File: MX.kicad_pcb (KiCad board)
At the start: 2 copper layers, 50.8 x 25.4 mm, 2 parts

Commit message: Fixed names
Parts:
- removed the SW** at (152.7, 88.9)
- added SW**: MX700H, Keyboard_switches:MX700H, F.Cu at (152.4, 88.9)
- moved LED** 0.25 mm to (152.4, 94.0)
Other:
- board size 50.8 x 25.4 mm -> 136.9 x 25.4 mm

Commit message: Upated MX700H and MX700HR
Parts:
- removed the SW** at (152.4, 88.9)
- added SW**: MX700HR, Keyboard_switches:MX700HR, F.Cu at (152.4, 88.9)

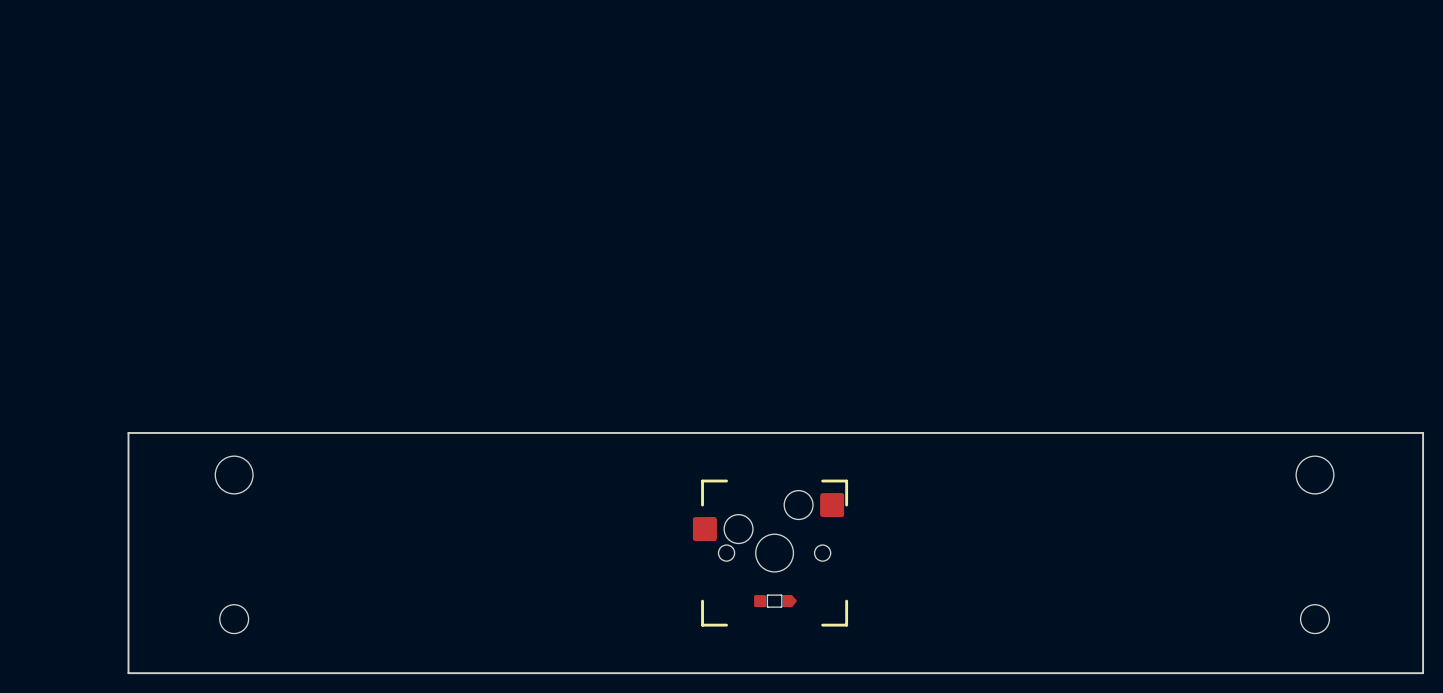
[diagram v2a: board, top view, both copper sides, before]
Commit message: Added symbols library
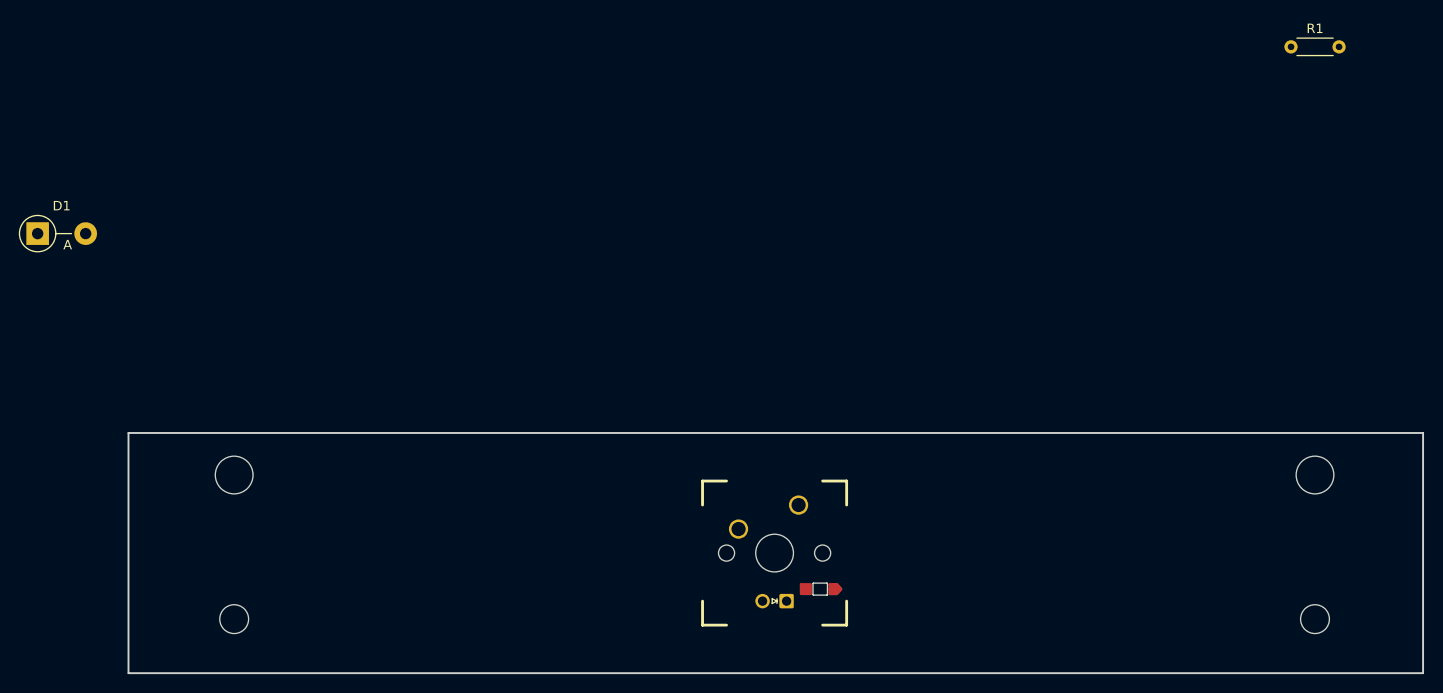
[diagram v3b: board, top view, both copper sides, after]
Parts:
- removed LED**: smdLed0805, Keyboard_switches:smdLed0805
- removed SW**: MX700HR, Keyboard_switches:MX700HR
- added D1: 1N4148, Diode_THT:D_DO-15_P5.08mm_Vertical_AnodeUp, F.Cu at (74.5, 55.1)
- added LED1: 0805, Keyboard_switches:smdLed0805, F.Cu at (157.2, 92.7)
- added R1: 100r, Resistor_THT:R_Axial_DIN0204_L3.6mm_D1.6mm_P5.08mm_Horizontal, F.Cu at (207.0, 35.4)
- added SW1: MXSwitch, Keyboard_switches:MX700R, F.Cu at (152.4, 88.9)

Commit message: Added support for THT LEDs
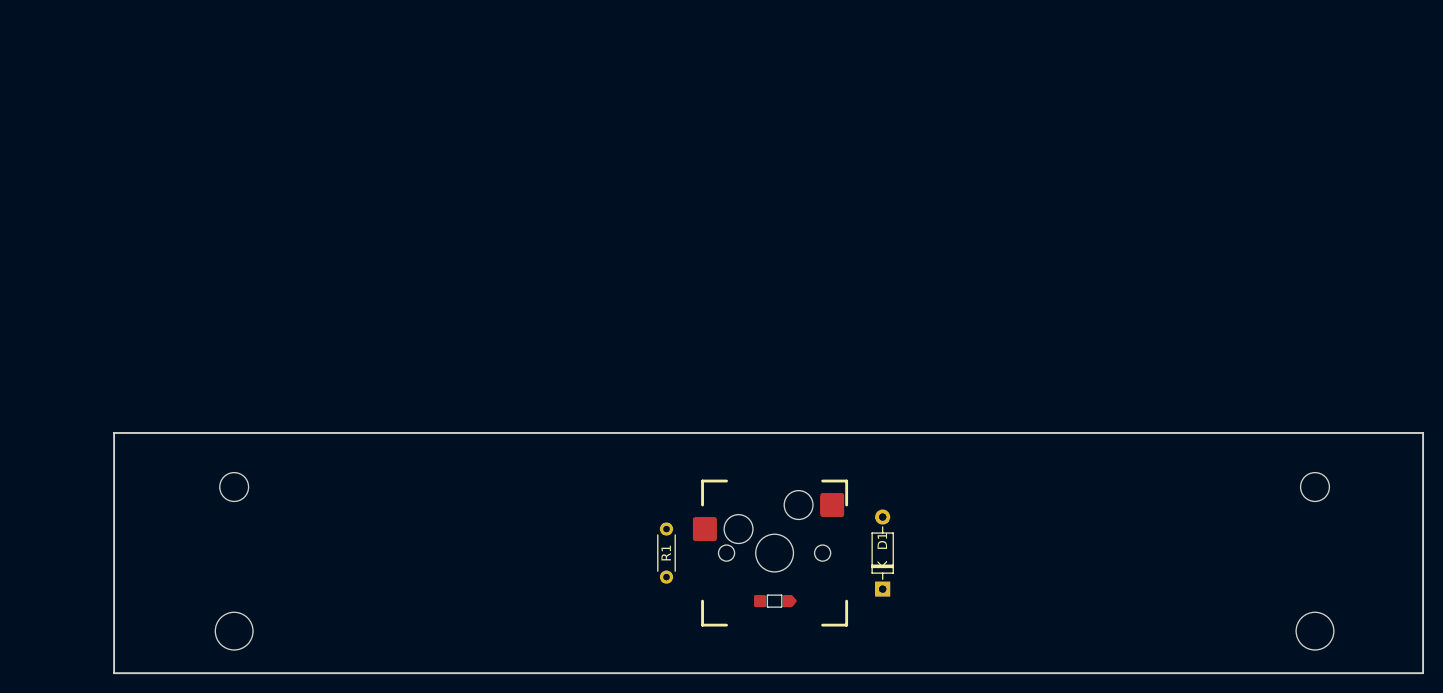
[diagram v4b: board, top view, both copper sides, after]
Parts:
- D1: footprint Diode_THT:D_DO-15_P5.08mm_Vertical_AnodeUp -> Diode_THT:D_DO-35_SOD27_P7.62mm_Horizontal
- LED1: value 0805 -> Red
- R1: value 100r -> 300R
- SW1: footprint Keyboard_switches:MX700R -> Keyboard_switches:MX700H
- moved D1 97.0 mm to (163.8, 92.7), turned to 90 degrees
- moved R1 83.4 mm to (141.0, 86.4), turned to 270 degrees
- moved LED1 4.99 mm to (152.4, 94.0)
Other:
- board size 136.9 x 25.4 mm -> 138.4 x 25.4 mm

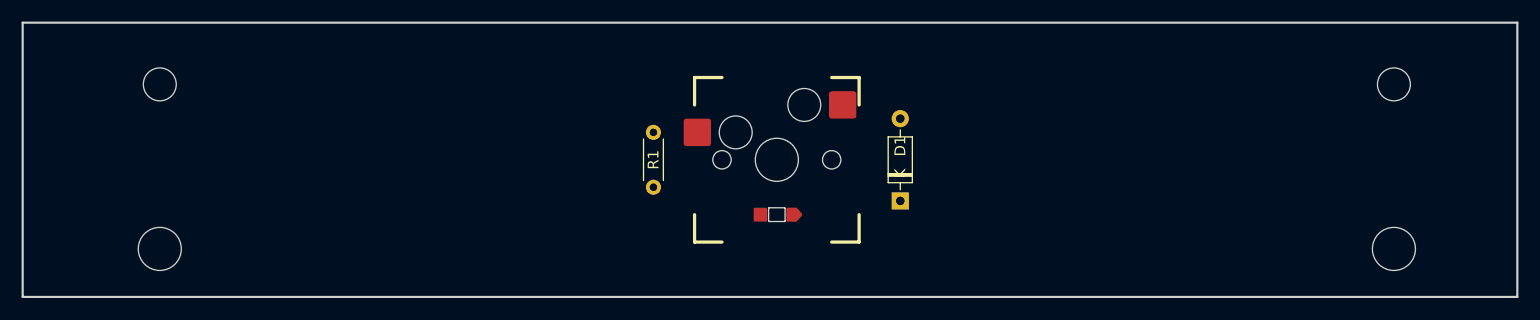
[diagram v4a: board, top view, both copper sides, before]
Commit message: Improved silkscreen markings, LED footprints and added diode footprint
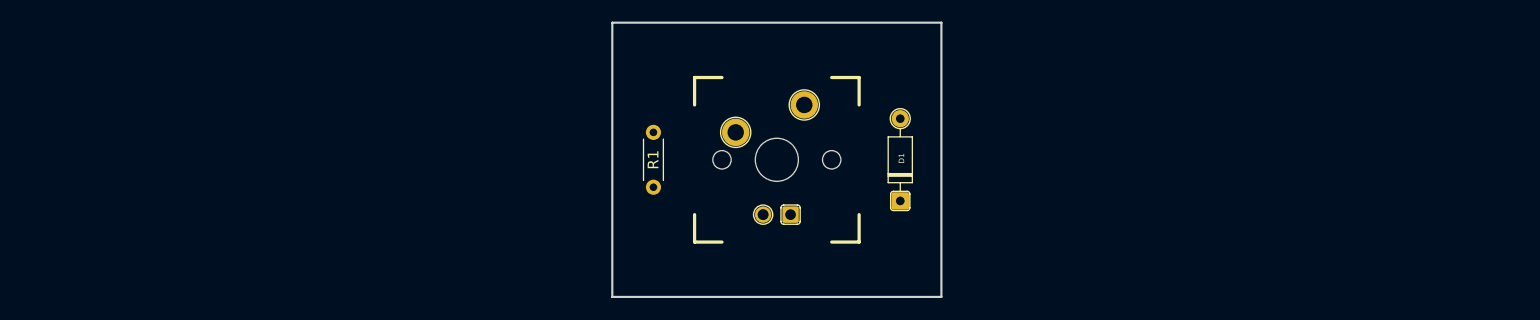
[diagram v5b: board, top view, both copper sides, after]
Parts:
- D1: footprint Diode_THT:D_DO-35_SOD27_P7.62mm_Horizontal -> Keyboard_switches:thtDiode
- LED1: footprint Keyboard_switches:smdLed0805 -> Keyboard_switches:thtLED
- SW1: footprint Keyboard_switches:MX700H -> Keyboard_switches:MX100
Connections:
- LED1 pad K: Net-(D1-Pad1) -> Net-(LED1-PadK)
- R1 pad 1: Net-(R1-Pad1) -> Net-(D1-Pad1)
- SW1 pad 1: Net-(D1-Pad2) -> Net-(LED1-PadK)
- SW1 pad 2: Net-(R1-Pad1) -> Net-(D1-Pad2)
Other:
- board size 138.4 x 25.4 mm -> 30.5 x 25.4 mm
